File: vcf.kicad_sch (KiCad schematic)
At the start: 0 parts

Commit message: modificato:             analog_synth.kicad_pro 	modificato:             key_encoder.kicad_sch 	modificato:             vca.kicad_pro 	modificato:             vca.kicad_sch 	nuovo file:             vca.net 	modificato:             vcf.kicad_sch
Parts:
- added C9: 30pF, symbol Device:C_Small
- added Q1: PNP, symbol Simulation_SPICE:PNP
- added R29, R30, R31: 270k, symbol Device:R
- added R32, R37: 150k, symbol Device:R
- added R33, R34: 470k, symbol Device:R
- added R35, R36: 330, symbol Device:R
- added RV3: 100k, symbol Device:R_Potentiometer
- added S21: SW_SPST, symbol Switch:SW_SPST
- added U6: LM301, symbol Amplifier_Operational:LM301
- added U7, U8: CA3080A, symbol Amplifier_Operational:CA3080A
- added U9: LM324, symbol Amplifier_Operational:LM324
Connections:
- new net: C9.1, U6.8 (C/B)
- new net: C9.2, U6.1 (BAL)
- new net: Q1.1 (C), R35.2, R36.2
- new net: R29.2, R30.2, R31.2, R32.1, U6.2 (-)
- new net: Q1.2 (B), U6.6
- new net: Q1.3 (E), R32.2, R37.1
- new net CNT1: R29.1
- new net CNT2: R30.1
- new net CNT3: R31.1
- new net GNDREF: RV3.1, S21.1 (A), U6.3 (+)
- new net IC3K: R34.1, R35.1
- new net IC4K: R33.1, R36.1
- new net INIT_FREQ: R37.2, RV3.2, RV3.3
- new net VCF_SW2: R33.2, R34.2, S21.2 (B)
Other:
- title: (none) -> Filtro 4730 PAIA

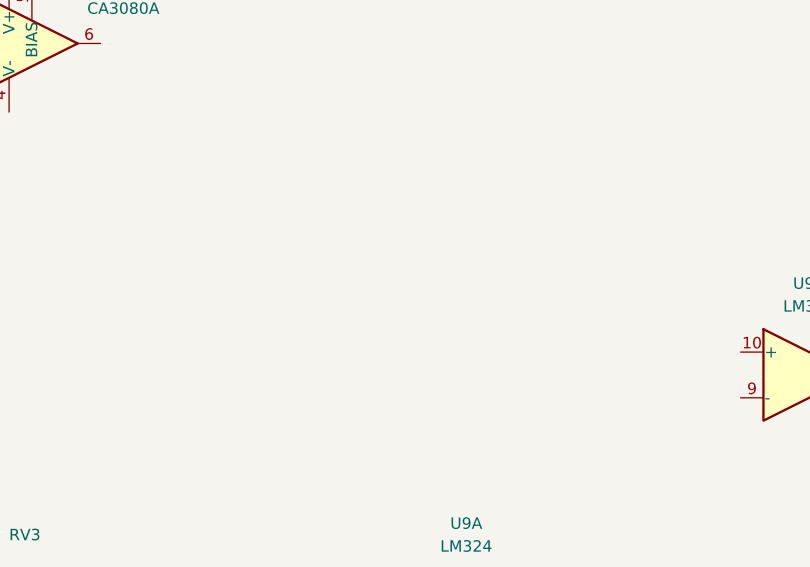
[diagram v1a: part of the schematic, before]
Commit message: eliminato:              adsr.kicad_pcb     eliminato:              adsr.kicad_pro 	modificato:             analog_synth.kicad_pcb 	nuovo file:             analog_synth.net 	eliminato:              audio_mixer.kicad_pcb 	eliminato:              audio_mixer.kicad_pro 	eliminato:              key_encoder.kicad_pcb 	eliminato:              key_encoder.kicad_pro 	modificato:             key_encoder.kicad_sch 	eliminato:              lfo.kicad_pcb 	eliminato:              lfo.kicad_pro 	eliminato:              noise_gen.kicad_pcb 	eliminato:              noise_gen.kicad_pro 	eliminato:              vca.kicad_pcb 	eliminato:              vca.kicad_prl 	eliminato:              vca.kicad_pro 	modificato:             vca.kicad_sch 	eliminato:              vca.net 	eliminato:              vcf.kicad_pcb 	eliminato:              vcf.kicad_prl 	eliminato:              vcf.kicad_pro 	modificato:             vcf.kicad_sch 	eliminato:              vco.kicad_pcb 	eliminato:              vco.kicad_pro
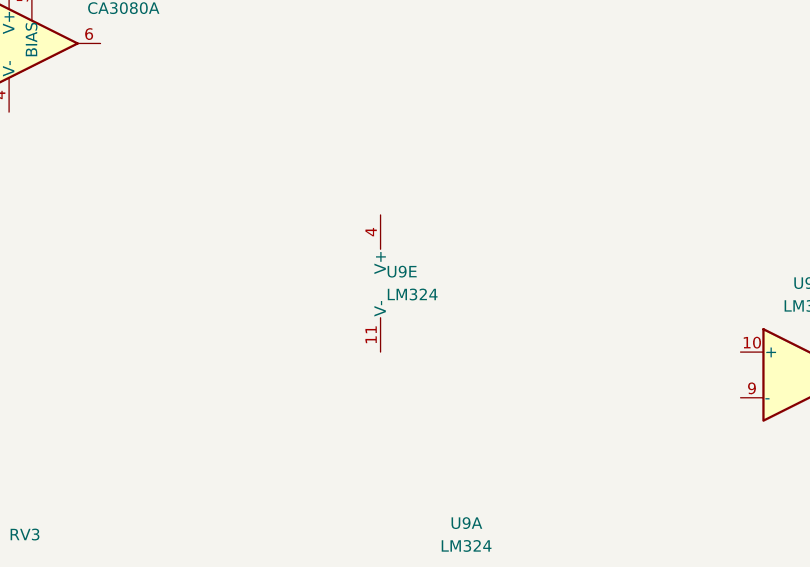
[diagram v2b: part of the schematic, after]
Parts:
- added unit 5 of U9
- R29, R30, R31, R32, R33, R34, R35, R36, R37, RV3: footprint (none) -> Resistor_SMD:R_0805_2012Metric
- U6, U7, U8: footprint (none) -> Package_DIP:DIP-8_W7.62mm_Socket
- U9: footprint (none) -> Package_DIP:DIP-14_W7.62mm_Socket
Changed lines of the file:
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@@
 			)
 		)
-		(property "Footprint" ""
+		(property "Footprint" "Resistor_SMD:R_0805_2012Metric"
 			(at 179.578 186.69 90)
 			(effects
@@
 			)
 		)
-		(property "Footprint" ""
+		(property "Footprint" "Resistor_SMD:R_0805_2012Metric"
 			(at 124.46 150.368 90)
 			(effects
@@
 			)
 		)
-		(property "Footprint" ""
+		(property "Footprint" "Package_DIP:DIP-8_W7.62mm_Socket"
 			(at 213.36 124.46 0)
 			(effects
@@
 			)
 		)
-		(property "Footprint" ""
+		(property "Footprint" "Resistor_SMD:R_0805_2012Metric"
 			(at 193.04 150.368 90)
 			(effects
@@
 			)
 		)
-		(property "Footprint" ""
+		(property "Footprint" "Resistor_SMD:R_0805_2012Metric"
 			(at 156.21 192.532 90)
 			(effects
@@
 			)
 		)
-		(property "Footprint" ""
+		(property "Footprint" "Package_DIP:DIP-14_W7.62mm_Socket"
 			(at 302.26 189.23 0)
 			(effects
@@
 			)
 		)
-		(property "Footprint" ""
+		(property "Footprint" "Resistor_SMD:R_0805_2012Metric"
 			(at 156.21 197.612 90)
 			(effects
@@
 			)
 		)
-		(property "Footprint" ""
+		(property "Footprint" "Resistor_SMD:R_0805_2012Metric"
 			(at 208.28 180.34 0)
 			(effects
@@
 			)
 		)
-		(property "Footprint" ""
+		(property "Footprint" "Resistor_SMD:R_0805_2012Metric"
 			(at 169.418 186.69 90)
 			(effects
@@
 			)
 		)
-		(property "Footprint" ""
+		(property "Footprint" "Resistor_SMD:R_0805_2012Metric"
 			(at 124.46 159.258 90)
 			(effects
@@
 			)
 		)
-		(property "Footprint" ""
+		(property "Footprint" "Package_DIP:DIP-8_W7.62mm_Socket"
 			(at 152.4 170.18 0)
 			(effects
@@
 			)
 		)
-		(property "Footprint" ""
+		(property "Footprint" "Package_DIP:DIP-14_W7.62mm_Socket"
 			(at 298.45 158.75 0)
 			(effects
@@
 			)
 		)
-		(property "Footprint" ""
+		(property "Footprint" "Package_DIP:DIP-8_W7.62mm_Socket"
 			(at 212.09 96.52 0)
 			(effects
@@
 	)
 	(symbol
+		(lib_id "Amplifier_Operational:LM324")
+		(at 254.635 151.13 0)
+		(unit 5)
+		(exclude_from_sim no)
+		(in_bom yes)
+		(on_board yes)
+		(dnp no)
+		(fields_autoplaced yes)
+		(property "Reference" "U9"
+			(at 252.73 149.8599 0)
+			(effects
+				(font
+					(size 1.27 1.27)
+				)
+				(justify left)
+			)
+		)
+		(property "Value" "LM324"
+			(at 252.73 152.3999 0)
+			(effects
+				(font
+					(size 1.27 1.27)
+				)
+				(justify left)
+			)
+		)
+		(property "Footprint" ""
+			(at 253.365 148.59 0)
+			(effects
+				(font
+					(size 1.27 1.27)
+				)
+				(hide yes)
+			)
+		)
+		(property "Datasheet" "http://www.ti.com/lit/ds/symlink/lm2902-n.pdf"
+			(at 255.905 146.05 0)
+			(effects
+				(font
+					(size 1.27 1.27)
+				)
+				(hide yes)
+			)
+		)
+		(property "Description" "Low-Power, Quad-Operational Amplifiers, DIP-14/SOIC-14/SSOP-14"
+			(at 254.635 151.13 0)
+			(effects
+				(font
+					(size 1.27 1.27)
+				)
+				(hide yes)
+			)
+		)
+		(pin "4"
+		)
+		(pin "5"
+		)
+		(pin "2"
+		)
+		(pin "13"
+		)
+		(pin "6"
+		)
+		(pin "10"
+		)
+		(pin "12"
+		)
+		(pin "9"
+		)
+		(pin "11"
+		)
+		(pin "3"
+		)
+		(pin "14"
+		)
+		(pin "1"
+		)
+		(pin "7"
+		)
+		(pin "8"
+		)
+		(instances
+			(project ""
+				(path "/ce123c18-2cf1-4c4e-87f3-498e0feabd95/3b667bbc-cd14-4848-b89b-2f70a2bfcac1"
+					(reference "U9")
+					(unit 5)
+				)
+			)
+		)
+	)
+	(symbol
 		(lib_id "Device:R")
 		(at 124.46 166.37 90)
@@
 			)
 		)
-		(property "Footprint" ""
+		(property "Footprint" "Resistor_SMD:R_0805_2012Metric"
 			(at 124.46 168.148 90)
 			(effects
@@
 			)
 		)
-		(property "Footprint" ""
+		(property "Footprint" "Package_DIP:DIP-14_W7.62mm_Socket"
 			(at 260.35 185.42 0)
 			(effects
@@
 			)
 		)
-		(property "Footprint" ""
+		(property "Footprint" "Resistor_SMD:R_0805_2012Metric"
 			(at 152.4 150.368 90)
 			(effects
